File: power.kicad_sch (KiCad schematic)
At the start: 12 parts, among them J2 Conn_01x08_Pin, U1 LFE5U-12F-6BG256C

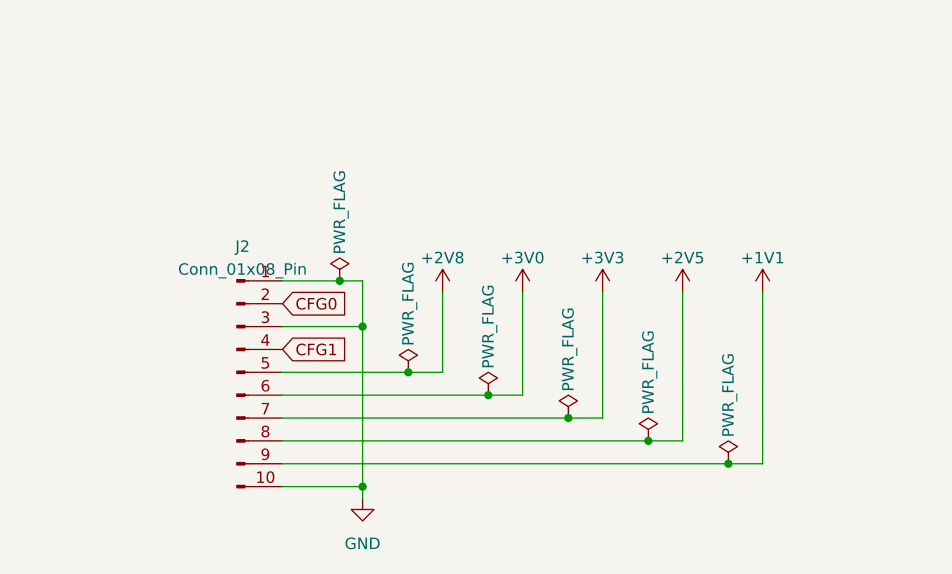
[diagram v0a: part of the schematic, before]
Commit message: Small routing tweaks, add breakout to schematic
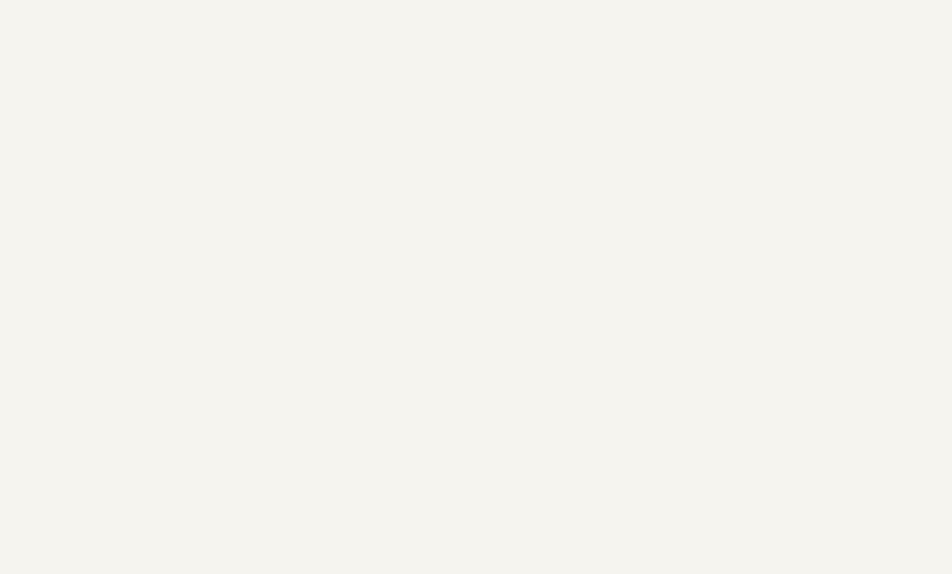
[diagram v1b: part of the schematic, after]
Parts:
- removed J2: Conn_01x08_Pin, Connector_PinHeader_2.54mm:PinHeader_2x05_P2.54mm_Vertical, symbol Connector:Conn_01x10_Pin

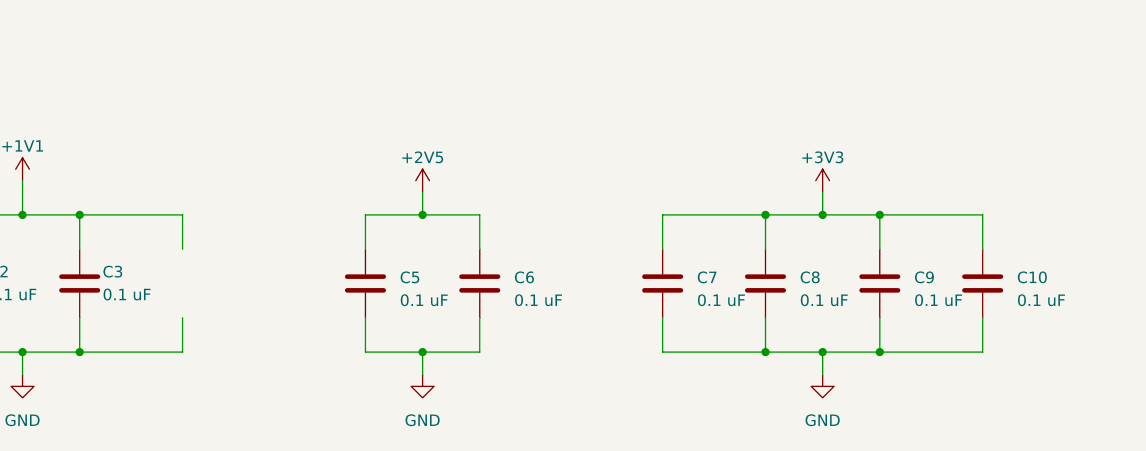
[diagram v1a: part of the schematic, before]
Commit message: Route flash + jtag resistors
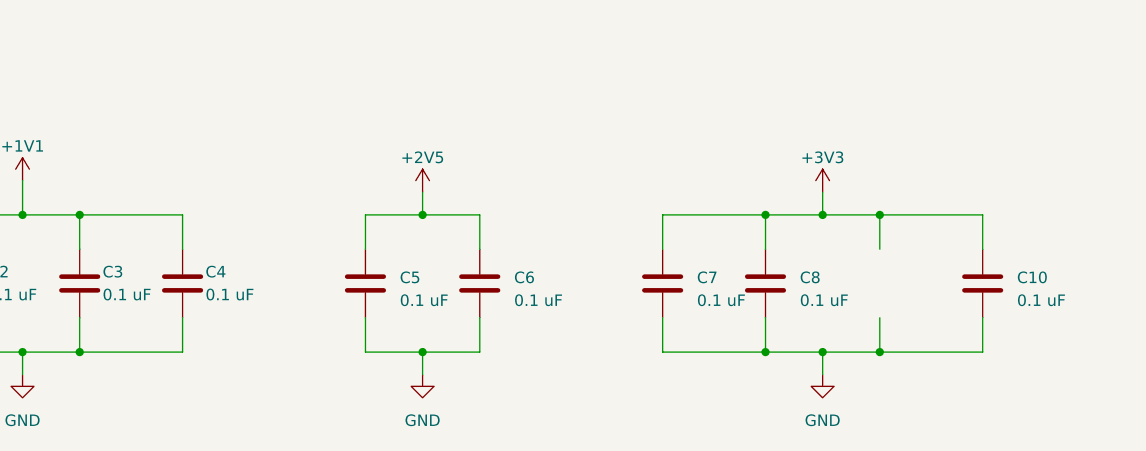
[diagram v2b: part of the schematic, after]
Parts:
- removed C9: 0.1 uF, Capacitor_SMD:C_0402_1005Metric, symbol Device:C
- added C4: 0.1 uF, Capacitor_SMD:C_0402_1005Metric, symbol Device:C
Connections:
- net +1V1: now also C4.1
- net GND: now also C4.2
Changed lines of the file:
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@@
+    )
+  )
+  (symbol (lib_id "Device:C") (at 100.33 80.01 0) (unit 1)
+    (in_bom yes) (on_board yes) (dnp no)
+    (property "Reference" "C4" (at 102.87 78.74 0)
+      (effects (font (size 1.27 1.27)) (justify left))
+    )
+    (property "Value" "0.1 uF" (at 102.87 81.28 0)
+      (effects (font (size 1.27 1.27)) (justify left))
+    )
+    (property "Footprint" "Capacitor_SMD:C_0402_1005Metric" (at 101.2952 83.82 0)
+      (effects (font (size 1.27 1.27)) hide)
+    )
+    (property "Datasheet" "~" (at 100.33 80.01 0)
+      (effects (font (size 1.27 1.27)) hide)
+    )
+    (pin "1")
+    (pin "2")
+    (instances
+      (project "daughterboard"
+        (path "/dce8b7ce-114c-4680-a1bd-14f36a94838a/233da297-15ca-4163-a51b-09f27dce3135"
+          (reference "C4") (unit 1)
+        )
+      )
     )
   )
@@
         )
       )
-    )
-  )
-  (symbol (lib_id "Device:C") (at 177.8 80.01 0) (unit 1)
-    (in_bom yes) (on_board yes) (dnp no) (fields_autoplaced)
-    (property "Reference" "C9" (at 181.61 79.375 0)
-      (effects (font (size 1.27 1.27)) (justify left))
-    )
-    (property "Value" "0.1 uF" (at 181.61 81.915 0)
-      (effects (font (size 1.27 1.27)) (justify left))
-    )
-    (property "Footprint" "Capacitor_SMD:C_0402_1005Metric" (at 178.7652 83.82 0)
-      (effects (font (size 1.27 1.27)) hide)
-    )
-    (property "Datasheet" "~" (at 177.8 80.01 0)
-      (effects (font (size 1.27 1.27)) hide)
-    )
-    (pin "1")
-    (pin "2")
-    (instances
-      (project "daughterboard"
-        (path "/dce8b7ce-114c-4680-a1bd-14f36a94838a/233da297-15ca-4163-a51b-09f27dce3135"
-          (reference "C9") (unit 1)
-        )
-      )

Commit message: Route power
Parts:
- added C13, C14, C15, C16, C17, C18: ~, Capacitor_SMD:C_0805_2012Metric, symbol Device:C
- added Q1, Q2: PMOS, Package_TO_SOT_SMD:SOT-23-3, symbol Simulation_SPICE:PMOS
- added Q3: NMOS, Package_TO_SOT_SMD:SOT-23-3, symbol Simulation_SPICE:NMOS
- added R17, R18, R19, R20, R21, R22: ~, Resistor_SMD:R_0805_2012Metric, symbol Device:R_US
- added U3: AMS1117-3.3, Package_TO_SOT_SMD:SOT-89-3, symbol Regulator_Linear:AMS1117-3.3
- added U4: TPS74611PQWDRBRQ1, Package_SON:Texas_S-PVSON-N8, symbol Regulator_Linear:TPS7A0508PDBV
- added U5: XC6206P252MR, Package_TO_SOT_SMD:SOT-23-3, symbol Regulator_Linear:AMS1117-3.3
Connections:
- net +1V1: now also C18.1, Q3.1 (D)
- net +2V5: now also C16.1, Q2.1 (D), R21.1
- net GND: now also R18.1, R19.1, U3.1 (GND), U4.4 (GND), U4.9 (PAD), U5.1 (GND)
- new net: C14.2, R17.1
- new net: C13.2, Q1.2 (G), R17.2, R18.2
- new net: C18.2, R22.1
- new net: C17.2, Q3.2 (G), R21.2, R22.2
- new net: C15.2, Q2.2 (G), R19.2, R20.2
- new net: C13.1, Q1.3 (S), U3.2 (VO)
- new net: C16.2, R20.1
- new net 1V1REGOUT: C17.1, Q3.3 (S), U4.1 (OUT)
- new net 2V5REGOUT: C15.1, Q2.3 (S), U5.2 (VO)
- new net 3V3REGIN: U4.5 (EN), U4.8 (IN), U5.3 (VI)
- new net 3V3REGOUT: C14.1, Q1.1 (D)
- new net 5VREGIN: U3.3 (VI)

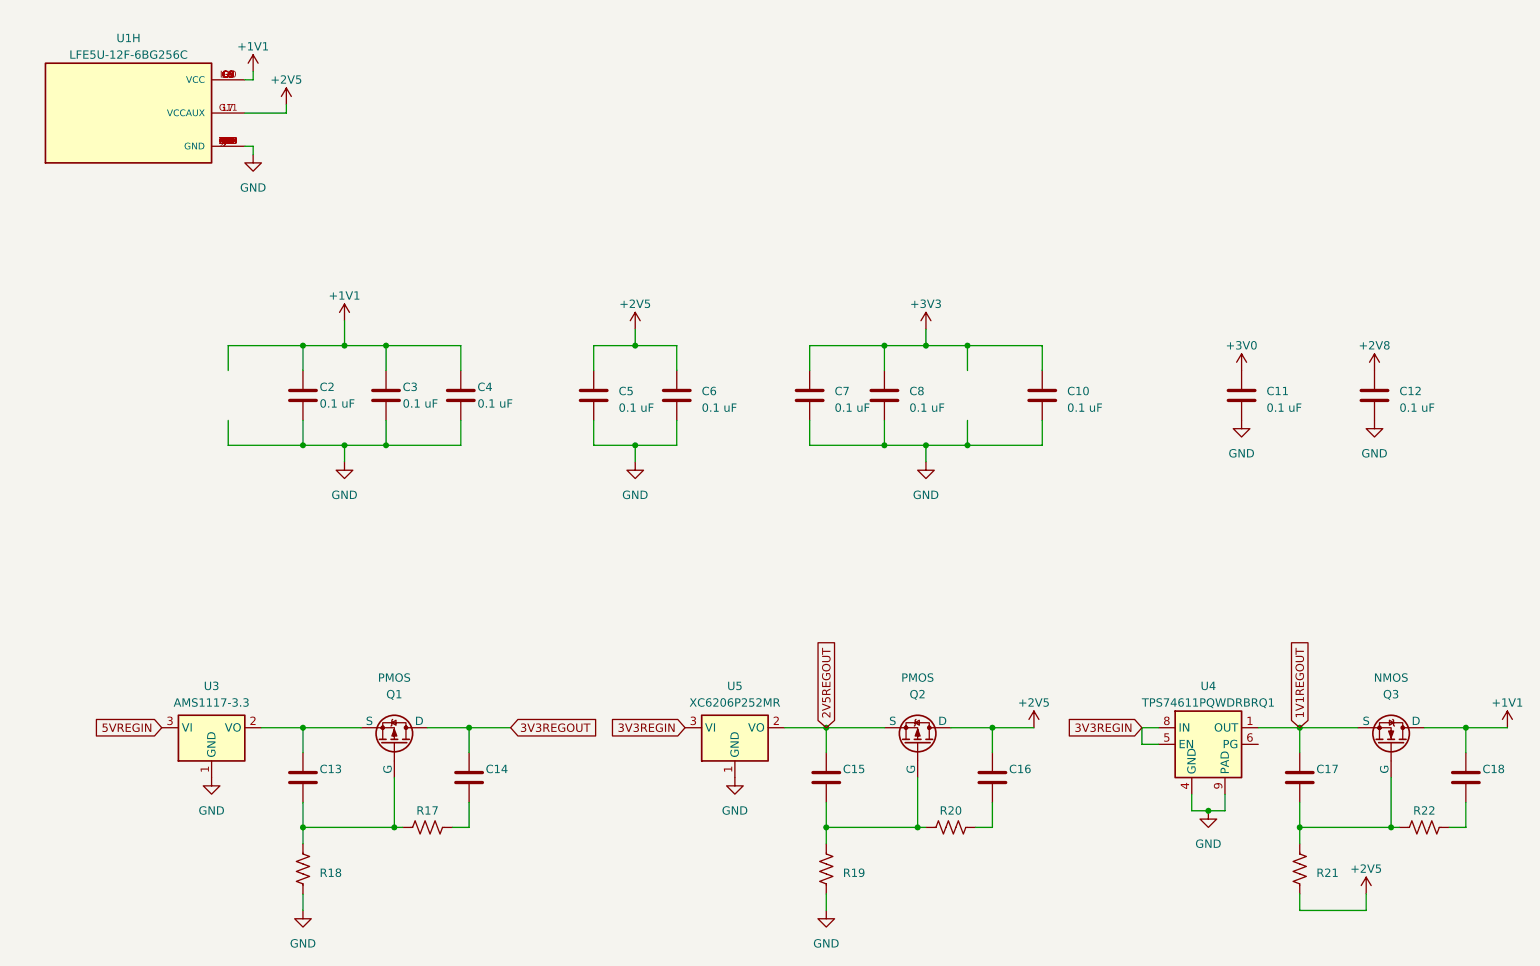
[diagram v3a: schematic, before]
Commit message: Schematic tweaks for readability
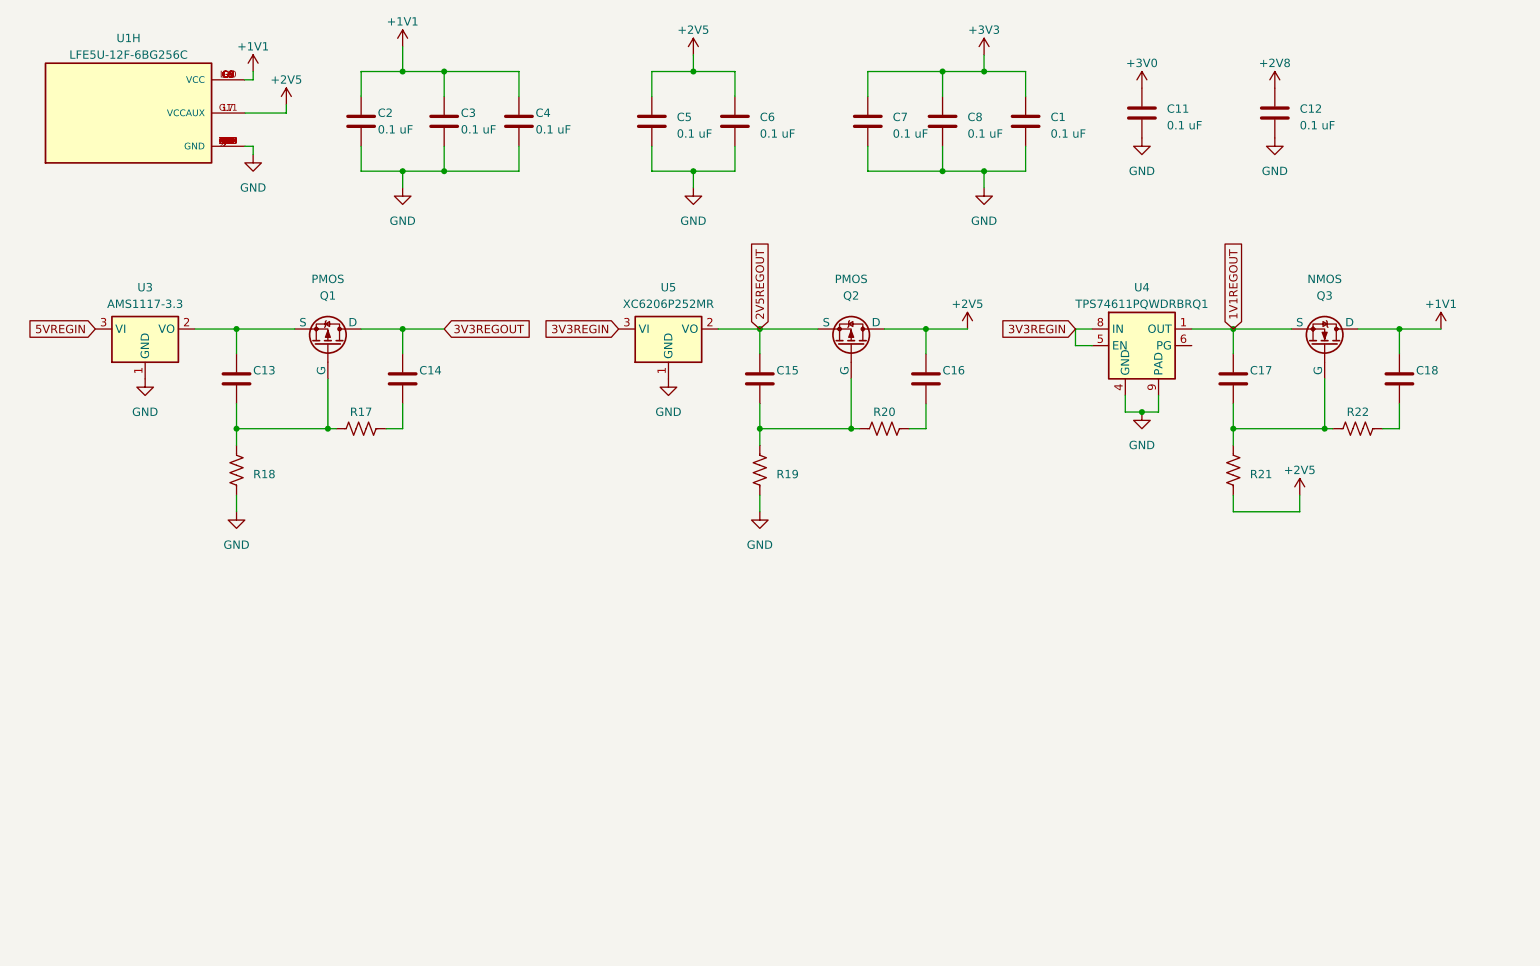
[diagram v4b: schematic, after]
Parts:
- removed C10: 0.1 uF, Capacitor_SMD:C_0402_1005Metric, symbol Device:C
- added C1: 0.1 uF, Capacitor_SMD:C_0402_1005Metric, symbol Device:C
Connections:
- net +3V3: now also C1.1
- net GND: now also C1.2
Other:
- moved on the sheet: C11, C12, C13, C14, C15, C16, C17, C18, C2, C3, C4, C5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

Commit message: Route power, FTDI chip
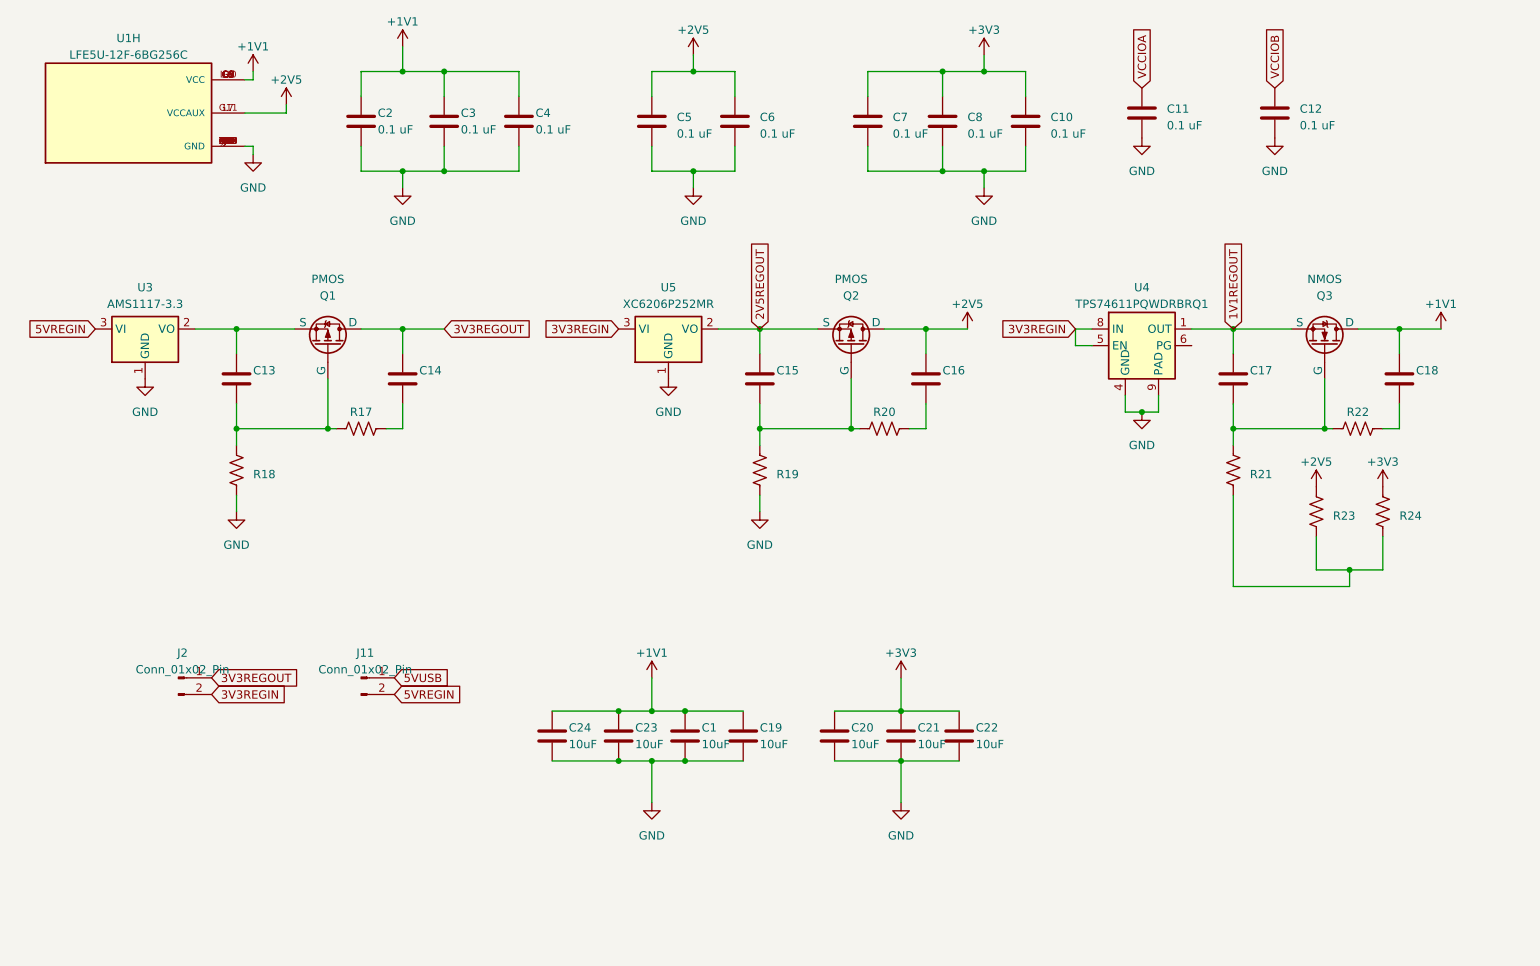
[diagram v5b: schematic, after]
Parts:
- added C10: 0.1 uF, Capacitor_SMD:C_0402_1005Metric, symbol Device:C
- added C19, C20, C21, C22, C23, C24: 10uF, Capacitor_SMD:C_0805_2012Metric, symbol Device:C
- added J11, J2: Conn_01x02_Pin, Connector_PinHeader_2.54mm:PinHeader_1x02_P2.54mm_Vertical, symbol Connector:Conn_01x02_Pin
- added R23, R24: ~, Resistor_SMD:R_0805_2012Metric, symbol Device:R_US
- C1: value 0.1 uF -> 10uF; footprint Capacitor_SMD:C_0402_1005Metric -> Capacitor_SMD:C_0805_2012Metric
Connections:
- net +1V1: now also C1.1, C19.1, C23.1, C24.1
- net +2V5: now also R23.2; no longer R21.1
- net +3V3: now also C10.1, C20.1, C21.1, C22.1, R24.2; no longer C1.1
- net 3V3REGIN: now also J2.2 (Pin_2)
- net 3V3REGOUT: now also J2.1 (Pin_1)
- net 5VREGIN: now also J11.2 (Pin_2)
- net GND: now also C10.2, C19.2, C20.2, C21.2, C22.2, C23.2, C24.2
- net +2V8 renamed VCCIOB
- net +3V0 renamed VCCIOA
- new net: R21.1, R23.1, R24.1
- new net 5VUSB: J11.1 (Pin_1)
